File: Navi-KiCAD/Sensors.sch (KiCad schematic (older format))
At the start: 12 parts, among them U5 MPU-9250, U7 LPS25HBTR

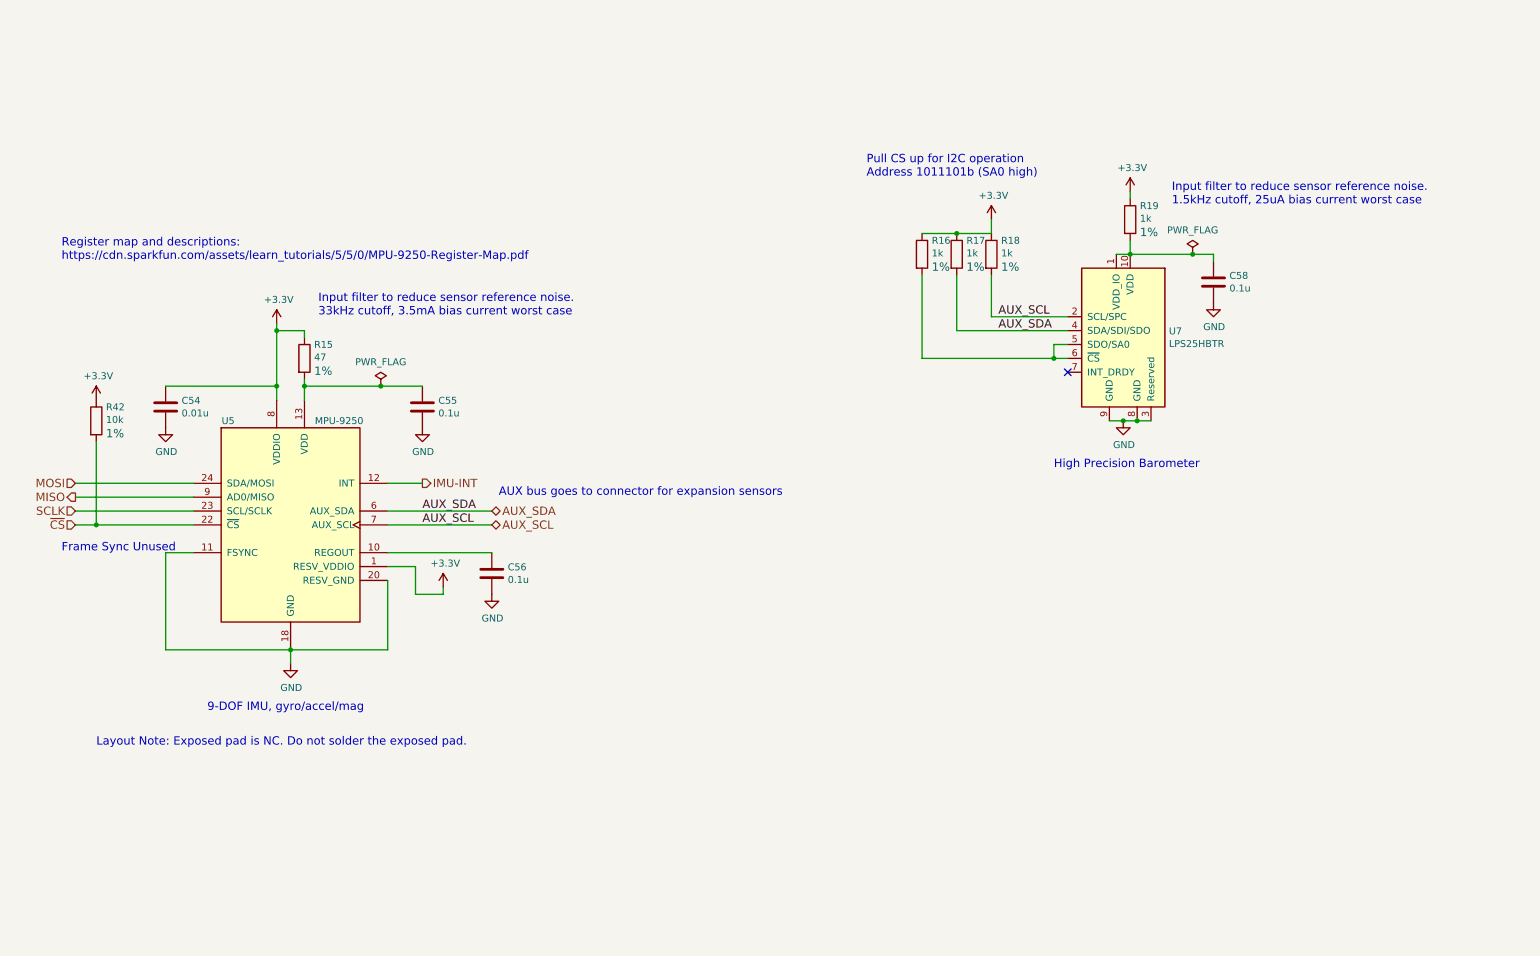
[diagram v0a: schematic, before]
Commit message: Completed key routing.
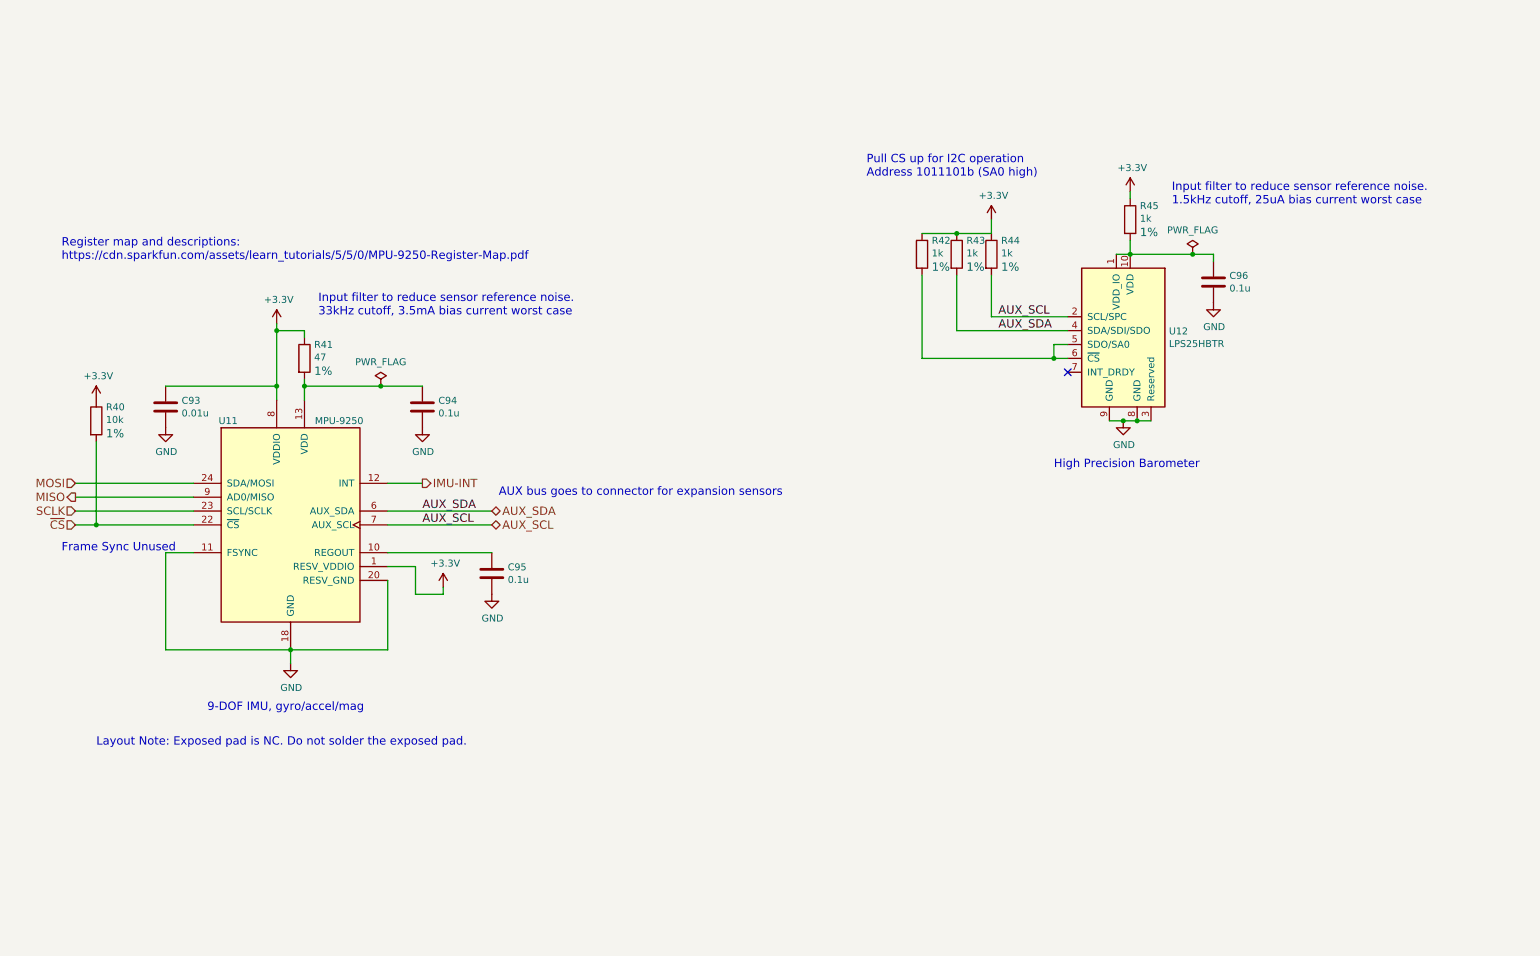
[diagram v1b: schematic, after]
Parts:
- renumbered C54 to C93, C55 to C94, C56 to C95, C58 to C96, R42 to R40, R15 to R41, R16 to R42, R17 to R43, R18 to R44, R19 to R45, U5 to U11, U7 to U12
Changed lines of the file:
@@
 $EndDescr
 $Comp
-L MPU-9250 U5
+L MPU-9250 U11
 U 1 1 58AB562F
 P 2400 4300
-F 0 "U5" H 1950 5050 50  0000 C CNN
+F 0 "U11" H 1950 5050 50  0000 C CNN
 F 1 "MPU-9250" H 2750 5050 50  0000 C CNN
 F 2 "Housings_DFN_QFN:QFN-24-1EP_3x3mm_Pitch0.4mm_MPU-9250" H -800 50  50  0001 C CNN
@@
 AUX_SDA
 $Comp
-L C C58
+L C C96
 U 1 1 58B4B88F
 P 9050 2550
-F 0 "C58" H 9165 2596 50  0000 L CNN
+F 0 "C96" H 9165 2596 50  0000 L CNN
 F 1 "0.1u" H 9165 2505 50  0000 L CNN
 F 2 "Capacitors_SMD:C_0402" H 2288 -1350 50  0001 C CNN
@@
 $EndComp
 $Comp
-L R R19
+L R R45
 U 1 1 58B4BB21
 P 8450 2100
-F 0 "R19" H 8520 2199 50  0000 L CNN
+F 0 "R45" H 8520 2199 50  0000 L CNN
 F 1 "1k" H 8520 2108 50  0000 L CNN
 F 2 "Resistors_SMD:R_0402" V 1000 450 50  0001 C CNN
@@
 $EndComp
 $Comp
-L R R18
+L R R44
 U 1 1 58B4C210
 P 7450 2350
-F 0 "R18" H 7520 2449 50  0000 L CNN
+F 0 "R44" H 7520 2449 50  0000 L CNN
 F 1 "1k" H 7520 2358 50  0000 L CNN
 F 2 "Resistors_SMD:R_0402" V 0   700 50  0001 C CNN
@@
 $EndComp
 $Comp
-L R R17
+L R R43
 U 1 1 58B4C26C
 P 7200 2350
-F 0 "R17" H 7270 2449 50  0000 L CNN
+F 0 "R43" H 7270 2449 50  0000 L CNN
 F 1 "1k" H 7270 2358 50  0000 L CNN
 F 2 "Resistors_SMD:R_0402" V -250 700 50  0001 C CNN
@@
 	3100 4300 3850 4300
 $Comp
-L R R16
+L R R42
 U 1 1 58B4CBDD
 P 6950 2350
-F 0 "R16" H 7020 2449 50  0000 L CNN
+F 0 "R42" H 7020 2449 50  0000 L CNN
 F 1 "1k" H 7020 2358 50  0000 L CNN
 F 2 "Resistors_SMD:R_0402" V -500 700 50  0001 C CNN
@@
 MOSI
 $Comp
-L R R15
+L R R41
 U 1 1 58B4F0B4
 P 2500 3100
-F 0 "R15" H 2570 3199 50  0000 L CNN
+F 0 "R41" H 2570 3199 50  0000 L CNN
 F 1 "47" H 2570 3108 50  0000 L CNN
 F 2 "Resistors_SMD:R_0402" V -800 1650 50  0001 C CNN
@@
 	2500 3250 2500 3400
 $Comp
-L C C55
+L C C94
 U 1 1 58B4F645
 P 3350 3450
-F 0 "C55" H 3465 3496 50  0000 L CNN
+F 0 "C94" H 3465 3496 50  0000 L CNN
 F 1 "0.1u" H 3465 3405 50  0000 L CNN
 F 2 "Capacitors_SMD:C_0402" H -3412 -450 50  0001 C CNN
@@
 $EndComp
 $Comp
-L C C54
+L C C93
 U 1 1 58B4F7C8
 P 1500 3450
-F 0 "C54" H 1615 3496 50  0000 L CNN
+F 0 "C93" H 1615 3496 50  0000 L CNN
 F 1 "0.01u" H 1615 3405 50  0000 L CNN
 F 2 "Capacitors_SMD:C_0402" H -5262 -450 50  0001 C CNN
@@
 $EndComp
 $Comp
-L C C56
+L C C95
 U 1 1 58B4FA48
 P 3850 4650
-F 0 "C56" H 3965 4696 50  0000 L CNN
+F 0 "C95" H 3965 4696 50  0000 L CNN
 F 1 "0.1u" H 3965 4605 50  0000 L CNN
 F 2 "Capacitors_SMD:C_0402" H -2912 750 50  0001 C CNN
@@
 Connection ~ 8900 2350
 $Comp
-L LPS25HB U7
+L LPS25HB U12
 U 1 1 58BE66D3
 P 8400 2950
-F 0 "U7" H 8071 2996 50  0000 R CNN
+F 0 "U12" H 8071 2996 50  0000 R CNN
 F 1 "LPS25HBTR" H 8071 2905 50  0000 R CNN
 F 2 "Housings_LGA:HLGA-10L_2.5x2.5mm_Pitch0.6mm" H -1250 1100 50  0001 C CIN
@@
 Connection ~ 8500 3550
 $Comp
-L R R42
+L R R40
 U 1 1 58D7F4C9
 P 1000 3550
-F 0 "R42" H 1070 3649 50  0000 L CNN
+F 0 "R40" H 1070 3649 50  0000 L CNN
 F 1 "10k" H 1070 3558 50  0000 L CNN
 F 2 "Resistors_SMD:R_0402" V -6450 1900 50  0001 C CNN

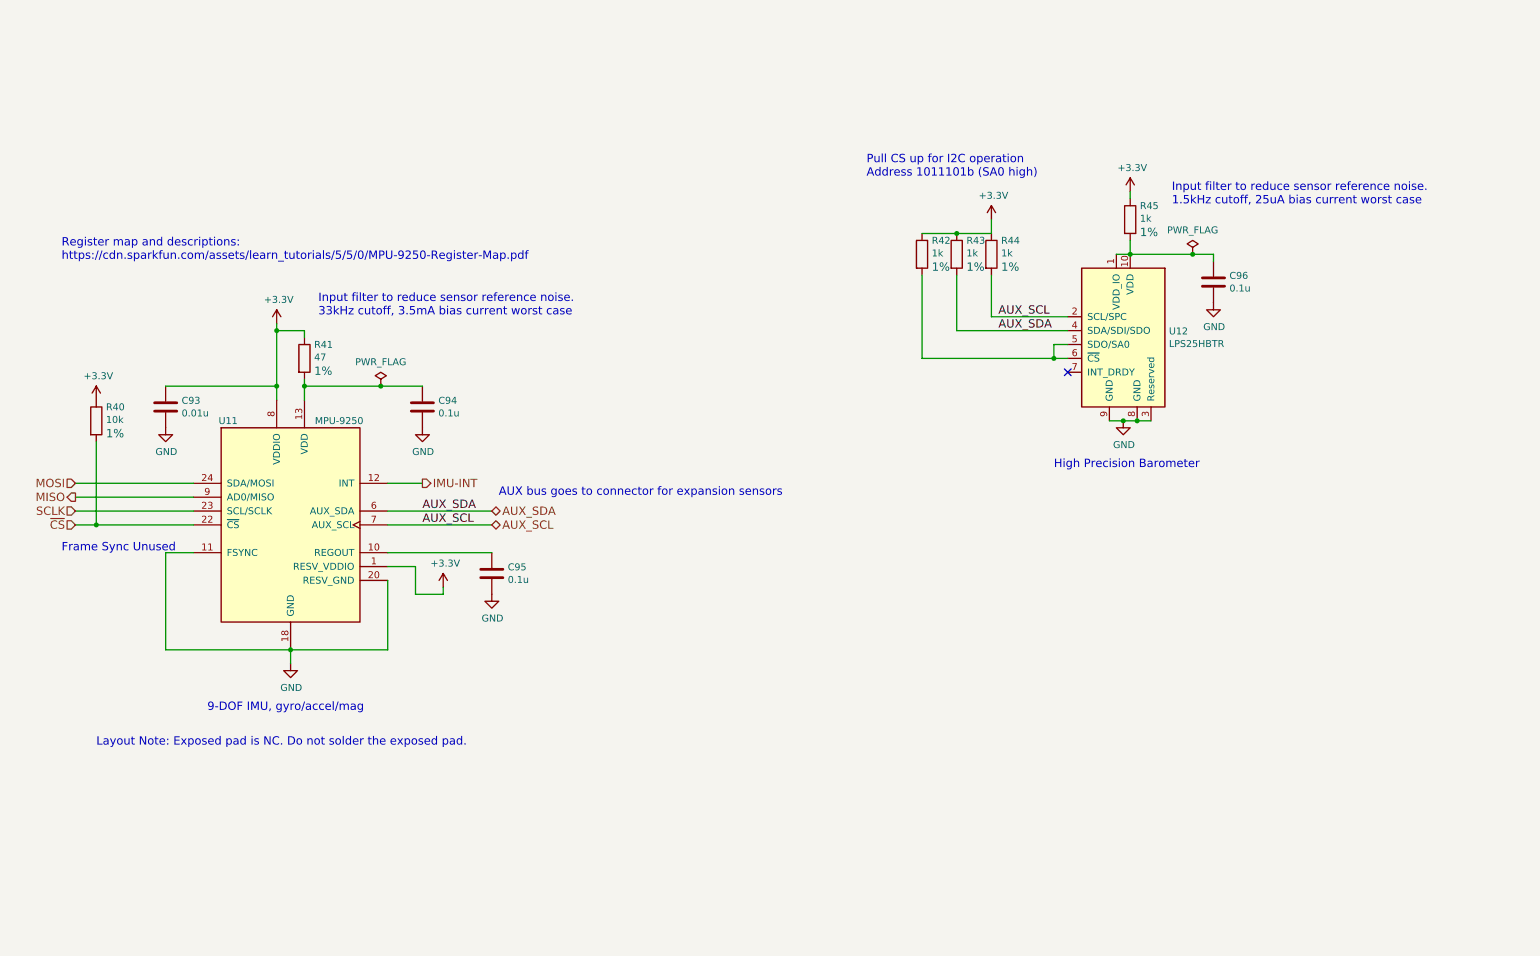
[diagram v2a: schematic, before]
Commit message: Upgraded to 9 channel RGB driver. Broke out signals for LSM303 and LSM6DS3
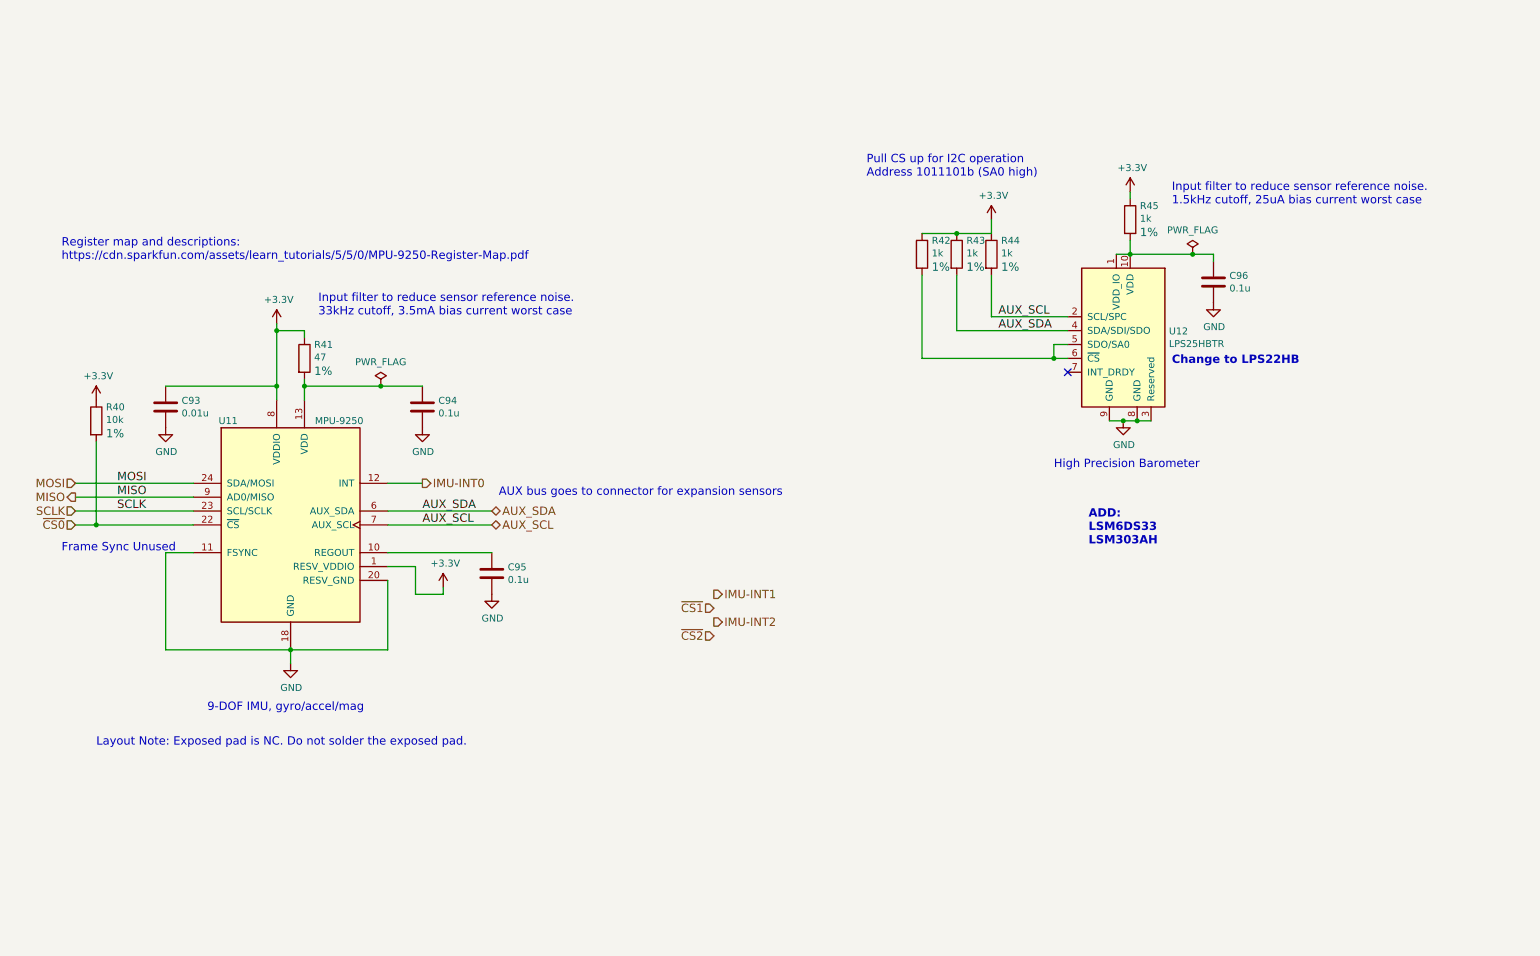
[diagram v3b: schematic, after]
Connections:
- net IMU-INT renamed IMU-INT0
- net ~CS renamed ~CS0
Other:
- note added: "ADD:\nLSM6DS33\nLSM303AH"
- note added: "Change to LPS22HB"
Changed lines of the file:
@@
 $EndComp
 $Comp
-L GND #PWR0141
+L GND #PWR98
 U 1 1 58B4AF5E
 P 2400 5300
-F 0 "#PWR0141" H -1950 1500 50  0001 C CNN
+F 0 "#PWR98" H -1950 1500 50  0001 C CNN
 F 1 "GND" H 2405 5127 50  0000 C CNN
 F 2 "" H -1950 1750 50  0001 C CNN
@@
 $EndComp
 $Comp
-L +3.3V #PWR0142
+L +3.3V #PWR97
 U 1 1 58B4AFA2
 P 2300 2850
-F 0 "#PWR0142" H -2200 -700 50  0001 C CNN
+F 0 "#PWR97" H -2200 -700 50  0001 C CNN
 F 1 "+3.3V" H 2315 3023 50  0000 C CNN
 F 2 "" H -2200 -550 50  0001 C CNN
@@
 $EndComp
 $Comp
-L GND #PWR0143
+L GND #PWR103
 U 1 1 58B4B105
 P 8400 3550
-F 0 "#PWR0143" H 4050 -250 50  0001 C CNN
+F 0 "#PWR103" H 4050 -250 50  0001 C CNN
 F 1 "GND" H 8405 3377 50  0000 C CNN
 F 2 "" H 4050 0   50  0001 C CNN
@@
 Connection ~ 8400 3550
 $Comp
-L +3.3V #PWR0144
+L +3.3V #PWR104
 U 1 1 58B4B14B
 P 8450 1900
-F 0 "#PWR0144" H 3950 -1650 50  0001 C CNN
+F 0 "#PWR104" H 3950 -1650 50  0001 C CNN
 F 1 "+3.3V" H 8465 2073 50  0000 C CNN
 F 2 "" H 3950 -1500 50  0001 C CNN
@@
 Connection ~ 8450 2350
 $Comp
-L GND #PWR0145
+L GND #PWR105
 U 1 1 58B4B9E9
 P 9050 2700
-F 0 "#PWR0145" H 4700 -1100 50  0001 C CNN
+F 0 "#PWR105" H 4700 -1100 50  0001 C CNN
 F 1 "GND" H 9055 2527 50  0000 C CNN
 F 2 "" H 4700 -850 50  0001 C CNN
@@
 Input filter to reduce sensor reference noise. \n1.5kHz cutoff, 25uA bias current worst case
 $Comp
-L +3.3V #PWR0146
+L +3.3V #PWR102
 U 1 1 58B4C158
 P 7450 2100
-F 0 "#PWR0146" H 2950 -1450 50  0001 C CNN
+F 0 "#PWR102" H 2950 -1450 50  0001 C CNN
 F 1 "+3.3V" H 7465 2273 50  0000 C CNN
 F 2 "" H 2950 -1300 50  0001 C CNN
@@
 9-DOF IMU, gyro/accel/mag
 Text HLabel 850  4300 0    60   Input ~ 0
-~CS
+~CS0
 Wire Wire Line
 	850  4300 1700 4300
@@
 	3100 4500 3850 4500
 $Comp
-L GND #PWR0147
+L GND #PWR101
 U 1 1 58B4FB3E
 P 3850 4800
-F 0 "#PWR0147" H -500 1000 50  0001 C CNN
+F 0 "#PWR101" H -500 1000 50  0001 C CNN
 F 1 "GND" H 3855 4627 50  0000 C CNN
 F 2 "" H -500 1250 50  0001 C CNN
@@
 	3500 4800 3500 4750
 $Comp
-L +3.3V #PWR0148
+L +3.3V #PWR100
 U 1 1 58B50137
 P 3500 4750
-F 0 "#PWR0148" H -1000 1200 50  0001 C CNN
+F 0 "#PWR100" H -1000 1200 50  0001 C CNN
 F 1 "+3.3V" H 3515 4923 50  0000 C CNN
 F 2 "" H -1000 1350 50  0001 C CNN
@@
 	3100 4000 3350 4000
 Text HLabel 3350 4000 2    60   Output ~ 0
-IMU-INT
-$Comp
-L GND #PWR0149
+IMU-INT0
+$Comp
+L GND #PWR99
 U 1 1 58B505FC
 P 3350 3600
-F 0 "#PWR0149" H -1000 -200 50  0001 C CNN
+F 0 "#PWR99" H -1000 -200 50  0001 C CNN
 F 1 "GND" H 3355 3427 50  0000 C CNN
 F 2 "" H -1000 50  50  0001 C CNN
@@
 Input filter to reduce sensor reference noise. \n33kHz cutoff, 3.5mA bias current worst case
 $Comp
-L GND #PWR0150
+L GND #PWR96
 U 1 1 58B50B96
 P 1500 3600
-F 0 "#PWR0150" H -2850 -200 50  0001 C CNN
+F 0 "#PWR96" H -2850 -200 50  0001 C CNN
 F 1 "GND" H 1505 3427 50  0000 C CNN
 F 2 "" H -2850 50  50  0001 C CNN
@@
 NoConn ~ 8000 3200
 $Comp
-L PWR_FLAG #FLG0151
+L PWR_FLAG #FLG13
 U 1 1 58BF1DC3
 P 3050 3300
-F 0 "#FLG0151" H -1800 125 50  0001 C CNN
+F 0 "#FLG13" H -1800 125 50  0001 C CNN
 F 1 "PWR_FLAG" H 3050 3474 50  0000 C CNN
 F 2 "" H -1800 50  50  0001 C CNN
@@
 Connection ~ 3050 3300
 $Comp
-L PWR_FLAG #FLG0152
+L PWR_FLAG #FLG14
 U 1 1 58BF1E5B
 P 8900 2350
-F 0 "#FLG0152" H 4050 -825 50  0001 C CNN
+F 0 "#FLG14" H 4050 -825 50  0001 C CNN
 F 1 "PWR_FLAG" H 8900 2524 50  0000 C CNN
 F 2 "" H 4050 -900 50  0001 C CNN
@@
 $EndComp
 $Comp
-L +3.3V #PWR0153
+L +3.3V #PWR95
 U 1 1 58D7F763
 P 1000 3400
-F 0 "#PWR0153" H -3500 -150 50  0001 C CNN
+F 0 "#PWR95" H -3500 -150 50  0001 C CNN
 F 1 "+3.3V" H 1015 3573 50  0000 C CNN
 F 2 "" H -3500 0   50  0001 C CNN
@@
 	1000 3700 1000 4300
 Connection ~ 1000 4300
+Text Notes 8150 4450 0    60   ~ 12
+ADD:\nLSM6DS33\nLSM303AH
+Text Notes 8750 3150 0    60   ~ 12
+Change to LPS22HB
+Text HLabel 5450 4800 2    60   Output ~ 0
+IMU-INT1
+Text HLabel 5450 4900 0    60   Input ~ 0
+~CS1
+Text HLabel 5450 5000 2    60   Output ~ 0
+IMU-INT2
+Text HLabel 5450 5100 0    60   Input ~ 0
+~CS2
+Text Label 1150 4000 0    60   ~ 0
+MOSI
+Text Label 1150 4100 0    60   ~ 0
+MISO
+Text Label 1150 4200 0    60   ~ 0
+SCLK
 $EndSCHEMATC
